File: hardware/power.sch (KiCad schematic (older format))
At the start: 56 parts, among them P1 CONN_01X02, P4 CONN_01X02, Q1 DMG4712SSS, Q2 DMG4712SSS, SW1 SPST, U10 LF33ABDT, U16 MCP1501T-30E, U17 MIC5225-5.0, U7 LT3471, U8 PDM1-S, U9 MIC5225-5.0

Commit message: Added most footprints, did non-power layout
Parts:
- removed SW1: SPST, symbol SPST
- added R55: 10k, symbol R
- added SW1: SW-SPST, 2kwMotorController:SW_SPST, symbol SW-SPST
- C62, C63: footprint (none) -> Capacitors_SMD:C_0603
- P1: value CONN_01X02 -> CONN_01X02_CBAT; footprint (none) -> 2kwMotorController:TERM_2P_2-5_1990009
- P4: value CONN_01X02 -> CONN_01X02_FAN; footprint (none) -> 2kwMotorController:TERM_2P_2-5_1990009
- R38, R39, R40, R41, R42, R54: footprint (none) -> Resistors_SMD:R_0603
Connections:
- wire segments 134 -> 137
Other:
- moved on the sheet: P1, Q1, R9
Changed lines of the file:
@@
 L CONN_01X02 P1
 U 1 1 597A960B
-P 800 1400
-F 0 "P1" H 800 1550 50  0000 C CNN
-F 1 "CONN_01X02" V 900 1400 50  0000 C CNN
-F 2 "" H 800 1400 50  0001 C CNN
-F 3 "" H 800 1400 50  0000 C CNN
-	1    800  1400
+P 950 1400
+F 0 "P1" H 950 1550 50  0000 C CNN
+F 1 "CONN_01X02_CBAT" V 1050 1400 50  0000 C CNN
+F 2 "2kwMotorController:TERM_2P_2-5_1990009" H 950 1400 50  0001 C CNN
+F 3 "" H 950 1400 50  0000 C CNN
+	1    950  1400
 	-1   0    0    -1
 $EndComp
-Text Notes 650  1050 0    60   ~ 12
+Text Notes 800  1050 0    60   ~ 12
 Battery Input\n9V max / 5V min\n750 mA max load\n2S LiPo Recommended
-$Comp
-L SPST SW1
-U 1 1 597A9A9C
-P 1550 1350
-F 0 "SW1" H 1550 1450 50  0000 C CNN
-F 1 "SPST" H 1550 1250 50  0000 C CNN
-F 2 "" H 1550 1350 50  0001 C CNN
-F 3 "" H 1550 1350 50  0000 C CNN
-	1    1550 1350
-	1    0    0    -1
-$EndComp
 $Comp
 L GND #PWR021
 U 1 1 597A9AEF
-P 2550 7350
-F 0 "#PWR021" H 2550 7100 50  0001 C CNN
-F 1 "GND" H 2550 7200 50  0000 C CNN
-F 2 "" H 2550 7350 50  0000 C CNN
-F 3 "" H 2550 7350 50  0000 C CNN
-	1    2550 7350
+P 2350 7350
+F 0 "#PWR021" H 2350 7100 50  0001 C CNN
+F 1 "GND" H 2350 7200 50  0000 C CNN
+F 2 "" H 2350 7350 50  0000 C CNN
+F 3 "" H 2350 7350 50  0000 C CNN
+	1    2350 7350
 	1    0    0    -1
 $EndComp
@@
 L R R9
 U 1 1 59870B9B
-P 2100 6800
-F 0 "R9" V 2180 6800 50  0000 C CNN
-F 1 "100" V 2100 6800 50  0000 C CNN
-F 2 "Resistors_SMD:R_0603" V 2030 6800 50  0001 C CNN
-F 3 "" H 2100 6800 50  0000 C CNN
-	1    2100 6800
-	1    0    0    -1
-$EndComp
-Text Notes 2350 7750 2    59   ~ 12
+P 1850 6750
+F 0 "R9" V 1930 6750 50  0000 C CNN
+F 1 "100" V 1850 6750 50  0000 C CNN
+F 2 "Resistors_SMD:R_0603" V 1780 6750 50  0001 C CNN
+F 3 "" H 1850 6750 50  0000 C CNN
+	1    1850 6750
+	-1   0    0    1
+$EndComp
+Text Notes 2500 7750 2    59   ~ 12
 REVERSE POLARITY PROTECTION\n14mW max - no heatsink needed
 Text Notes 8100 5650 0    60   ~ 12
@@
 F 0 "R38" V 4830 2300 50  0000 C CNN
 F 1 "220" V 4750 2300 50  0000 C CNN
-F 2 "" V 4680 2300 50  0001 C CNN
+F 2 "Resistors_SMD:R_0603" V 4680 2300 50  0001 C CNN
 F 3 "" H 4750 2300 50  0000 C CNN
 	1    4750 2300
@@
 F 0 "R39" V 6530 5000 50  0000 C CNN
 F 1 "2.2k" V 6450 5000 50  0000 C CNN
-F 2 "" V 6380 5000 50  0001 C CNN
+F 2 "Resistors_SMD:R_0603" V 6380 5000 50  0001 C CNN
 F 3 "" H 6450 5000 50  0000 C CNN
 	1    6450 5000
@@
 F 0 "R40" V 6530 6300 50  0000 C CNN
 F 1 "2.2k" V 6450 6300 50  0000 C CNN
-F 2 "" V 6380 6300 50  0001 C CNN
+F 2 "Resistors_SMD:R_0603" V 6380 6300 50  0001 C CNN
 F 3 "" H 6450 6300 50  0000 C CNN
 	1    6450 6300
@@
 $EndComp
 $Comp
-L GND #PWR046
+L GND #PWR045
 U 1 1 59BF3490
 P 2500 3500
-F 0 "#PWR046" H 2500 3250 50  0001 C CNN
+F 0 "#PWR045" H 2500 3250 50  0001 C CNN
 F 1 "GND" H 2500 3350 50  0000 C CNN
 F 2 "" H 2500 3500 50  0000 C CNN
@@
 $EndComp
 Wire Wire Line
-	1050 1350 1000 1350
-Wire Wire Line
-	1000 1450 1100 1450
-Wire Wire Line
-	2050 1350 3500 1350
+	1150 1350 3500 1350
+Wire Wire Line
+	1150 1450 1250 1450
 Wire Wire Line
 	2550 1350 2550 1250
@@
 	8750 4750 8750 4800
 Wire Wire Line
-	8750 5100 8750 5150
+	8750 5150 8750 5100
 Wire Wire Line
 	8200 5150 9200 5150
@@
 Connection ~ 8750 4300
 Wire Wire Line
-	1100 1450 1100 7350
-Wire Wire Line
-	1100 7300 1900 7300
-Wire Wire Line
-	2550 7300 2550 7350
-Wire Wire Line
-	2100 1300 2100 6650
+	1250 1450 1250 7350
+Wire Wire Line
+	1250 7300 1650 7300
+Wire Wire Line
+	2350 6950 2350 7350
+Wire Wire Line
+	2100 1300 2100 6550
 Connection ~ 2100 1350
 Wire Wire Line
-	2100 7000 2100 6950
-Wire Wire Line
-	2300 7300 2550 7300
+	2050 7300 2350 7300
 Wire Notes Line
 	7900 4650 7900 5750
@@
 Connection ~ 2550 1350
 Connection ~ 3150 1350
-Connection ~ 2100 6550
 Connection ~ 2100 4350
 Connection ~ 5850 4350
 Wire Wire Line
-	2400 5850 2100 5850
+	1850 5850 2400 5850
 Connection ~ 2100 5850
 Wire Wire Line
@@
 	2500 3450 2750 3450
 $Comp
-L +5V #PWR047
+L +5V #PWR046
 U 1 1 59BF5180
 P 3800 3100
-F 0 "#PWR047" H 3800 2950 50  0001 C CNN
+F 0 "#PWR046" H 3800 2950 50  0001 C CNN
 F 1 "+5V" H 3800 3240 50  0000 C CNN
 F 2 "" H 3800 3100 50  0000 C CNN
@@
 Encoder supply
 $Comp
-L GNDCBAT #PWR048
+L GNDCBAT #PWR047
 U 1 1 59C0C795
-P 1100 7350
-F 0 "#PWR048" H 1100 7100 50  0001 C CNN
-F 1 "GNDCBAT" H 1100 7200 50  0000 C CNN
-F 2 "" H 1100 7350 50  0000 C CNN
-F 3 "" H 1100 7350 50  0000 C CNN
-	1    1100 7350
-	1    0    0    -1
-$EndComp
-Connection ~ 1100 7300
+P 1250 7350
+F 0 "#PWR047" H 1250 7100 50  0001 C CNN
+F 1 "GNDCBAT" H 1250 7200 50  0000 C CNN
+F 2 "" H 1250 7350 50  0000 C CNN
+F 3 "" H 1250 7350 50  0000 C CNN
+	1    1250 7350
+	1    0    0    -1
+$EndComp
+Connection ~ 1250 7300
 Wire Wire Line
 	10150 2200 10150 2400
 $Comp
-L GND #PWR049
+L GND #PWR048
 U 1 1 59C60D75
 P 10150 2400
-F 0 "#PWR049" H 10150 2150 50  0001 C CNN
+F 0 "#PWR048" H 10150 2150 50  0001 C CNN
 F 1 "GND" H 10150 2250 50  0000 C CNN
 F 2 "" H 10150 2400 50  0000 C CNN
@@
 P 9650 1550
 F 0 "P4" H 9650 1700 50  0000 C CNN
-F 1 "CONN_01X02" V 9750 1550 50  0000 C CNN
-F 2 "" H 9650 1550 50  0001 C CNN
+F 1 "CONN_01X02_FAN" V 9750 1550 50  0000 C CNN
+F 2 "2kwMotorController:TERM_2P_2-5_1990009" H 9650 1550 50  0001 C CNN
 F 3 "" H 9650 1550 50  0000 C CNN
 	1    9650 1550
@@
 	10150 1700 10150 1800
 $Comp
-L +12V #PWR050
+L +12V #PWR049
 U 1 1 59C60D8A
 P 10150 1300
-F 0 "#PWR050" H 10150 1150 50  0001 C CNN
+F 0 "#PWR049" H 10150 1150 50  0001 C CNN
 F 1 "+12V" H 10150 1440 50  0000 C CNN
 F 2 "" H 10150 1300 50  0000 C CNN
@@
 F 0 "R41" V 9680 2000 50  0000 C CNN
 F 1 "100" V 9600 2000 50  0000 C CNN
-F 2 "" V 9530 2000 50  0001 C CNN
+F 2 "Resistors_SMD:R_0603" V 9530 2000 50  0001 C CNN
 F 3 "" H 9600 2000 50  0000 C CNN
 	1    9600 2000
@@
 F 0 "R42" V 9880 2200 50  0000 C CNN
 F 1 "10k" V 9800 2200 50  0000 C CNN
-F 2 "" V 9730 2200 50  0001 C CNN
+F 2 "Resistors_SMD:R_0603" V 9730 2200 50  0001 C CNN
 F 3 "" H 9800 2200 50  0000 C CNN
 	1    9800 2200
@@
 L NMOS_8PIN Q1
 U 1 1 59BDA6D3
-P 2100 7200
-F 0 "Q1" V 2100 7450 50  0000 R CNN
-F 1 "DMG4712SSS" V 2350 7400 50  0000 R CNN
-F 2 "Housings_SOIC:SOIC-8_3.9x4.9mm_Pitch1.27mm" H 2300 7300 50  0001 C CNN
-F 3 "" H 2100 7200 50  0000 C CNN
-	1    2100 7200
+P 1850 7200
+F 0 "Q1" V 1850 7450 50  0000 R CNN
+F 1 "DMG4712SSS" V 2100 7400 50  0000 R CNN
+F 2 "Housings_SOIC:SOIC-8_3.9x4.9mm_Pitch1.27mm" H 2050 7300 50  0001 C CNN
+F 3 "" H 1850 7200 50  0000 C CNN
+	1    1850 7200
 	0    -1   1    0
 $EndComp
@@
 F 0 "C62" H 7225 4650 50  0000 L CNN
 F 1 "2.2u" H 7225 4450 50  0000 L CNN
-F 2 "" H 7238 4400 50  0001 C CNN
+F 2 "Capacitors_SMD:C_0603" H 7238 4400 50  0001 C CNN
 F 3 "" H 7200 4550 50  0000 C CNN
 	1    7200 4550
@@
 F 0 "C63" H 8375 4650 50  0000 L CNN
 F 1 "2.2u" H 8375 4450 50  0000 L CNN
-F 2 "" H 8388 4400 50  0001 C CNN
+F 2 "Capacitors_SMD:C_0603" H 8388 4400 50  0001 C CNN
 F 3 "" H 8350 4550 50  0000 C CNN
 	1    8350 4550
@@
 F 0 "R54" V 8630 4950 50  0000 C CNN
 F 1 "2.2k" V 8550 4950 50  0000 C CNN
-F 2 "" V 8480 4950 50  0001 C CNN
+F 2 "Resistors_SMD:R_0603" V 8480 4950 50  0001 C CNN
 F 3 "" H 8550 4950 50  0000 C CNN
 	1    8550 4950
@@
 Connection ~ 8550 5150
 $Comp
-L GND #PWR?
+L GND #PWR050
 U 1 1 59BAC5F2
 P 3800 3550
-F 0 "#PWR?" H 3800 3300 50  0001 C CNN
+F 0 "#PWR050" H 3800 3300 50  0001 C CNN
 F 1 "GND" H 3800 3400 50  0000 C CNN
 F 2 "" H 3800 3550 50  0000 C CNN
@@
 	1    0    0    -1
 $EndComp
+Wire Wire Line
+	1850 6900 1850 7000
+$Comp
+L SW-SPST SW1
+U 1 1 59BC78B3
+P 1850 6200
+F 0 "SW1" H 1850 6300 50  0000 C CNN
+F 1 "SW-SPST" H 1850 6100 50  0000 C CNN
+F 2 "2kwMotorController:SW_SPST" H 1850 6200 50  0001 C CNN
+F 3 "" H 1850 6200 50  0000 C CNN
+	1    1850 6200
+	0    1    1    0
+$EndComp
+Wire Wire Line
+	1850 6600 1850 6500
+Wire Wire Line
+	1850 5900 1850 5850
+$Comp
+L R R55
+U 1 1 59BCE5FC
+P 2150 6950
+F 0 "R55" V 2230 6950 50  0000 C CNN
+F 1 "10k" V 2150 6950 50  0000 C CNN
+F 2 "" V 2080 6950 50  0001 C CNN
+F 3 "" H 2150 6950 50  0000 C CNN
+	1    2150 6950
+	0    1    1    0
+$EndComp
+Wire Wire Line
+	2350 6950 2300 6950
+Connection ~ 2350 7300
+Wire Wire Line
+	1850 6950 2000 6950
+Connection ~ 1850 6950
 $EndSCHEMATC

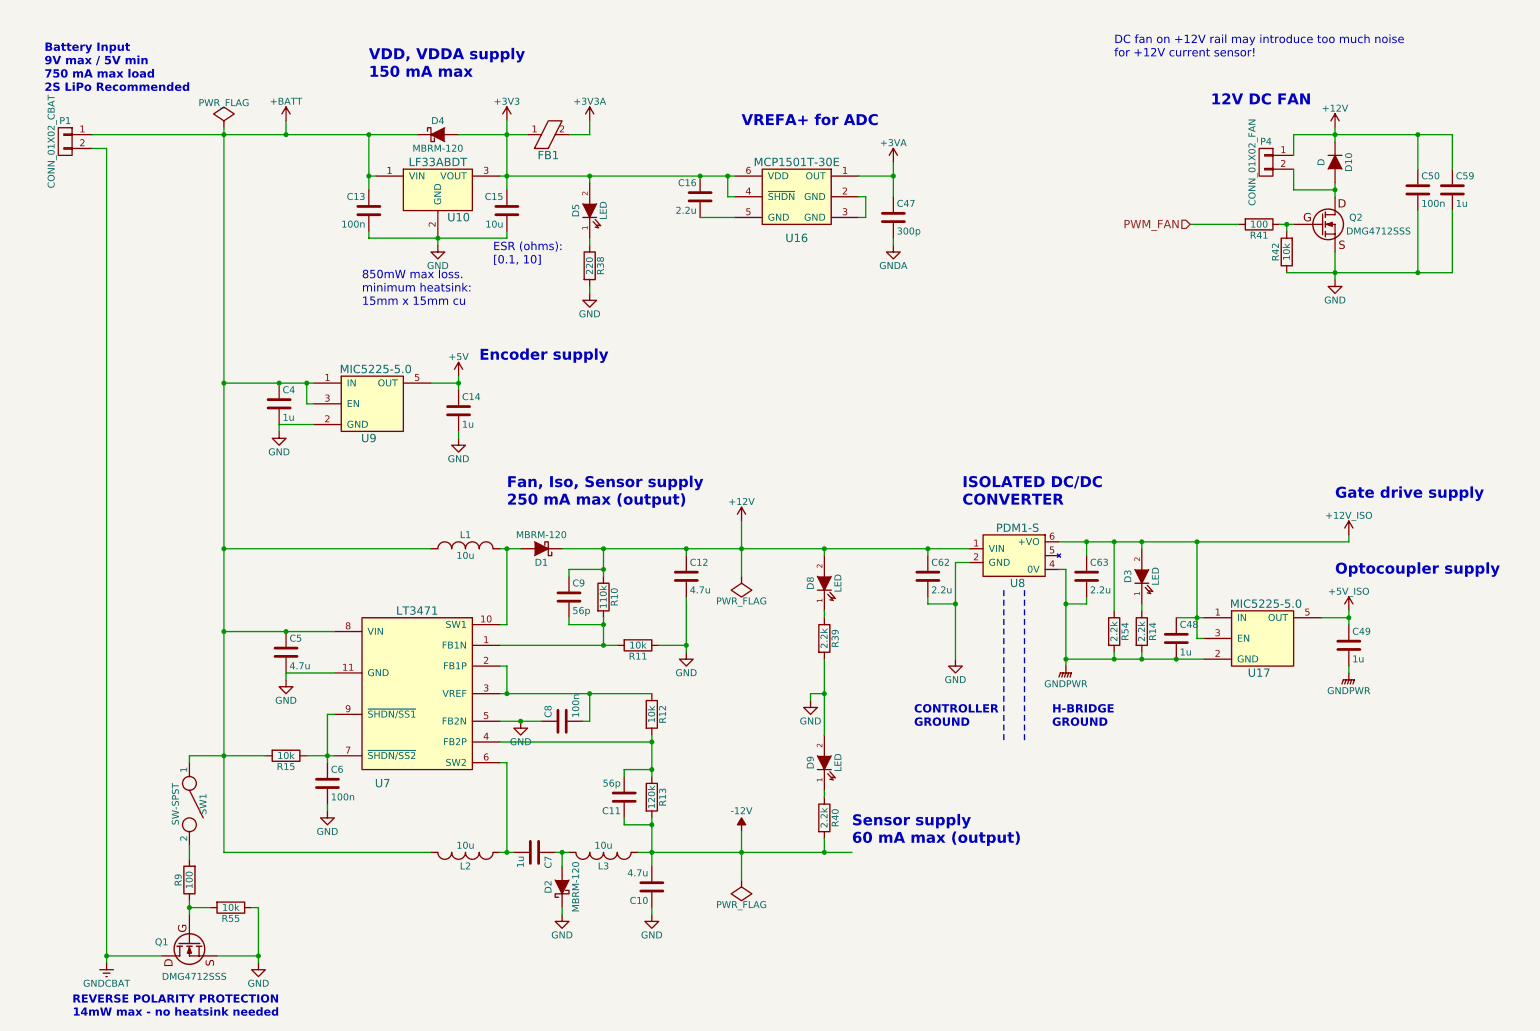
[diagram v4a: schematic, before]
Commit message: H-bridge decoupling, footprints, mechanical
- Finished H-bridge decoupling study and chose H-bridge caps
- Changed LT3471 inductors to those found in reference design,
  made footprints for them
- Swapped Si86xx isolator for Si80xx (smaller package)
- Updated heatsink footprint with correct screw sizes
- Created mechanical hole footprints (M3, M4 screws)
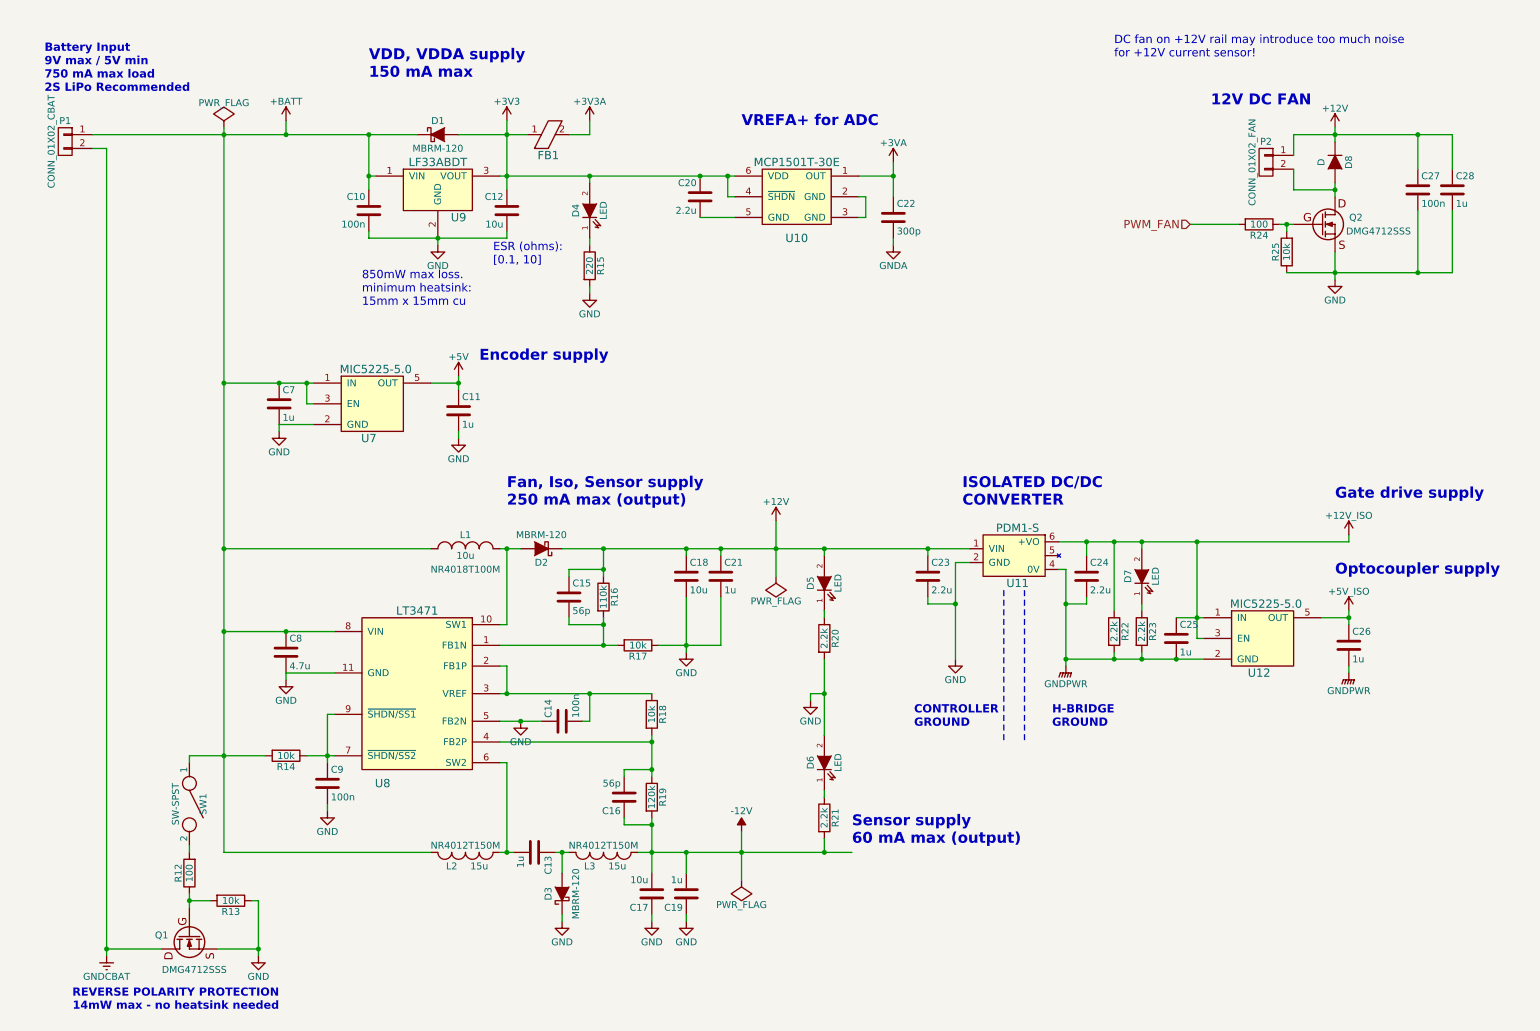
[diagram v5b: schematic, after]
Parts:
- added C19, C21: 1u, Capacitors_SMD:C_0603, symbol C
- C17: renamed from C10; value 4.7u -> 10u
- C18: renamed from C12; value 4.7u -> 10u
- L1: footprint Capacitors_SMD:C_0603 -> 2kwMotorController:INDUCTOR_NR40xx
- L2, L3: value 10u -> 15u; footprint Capacitors_SMD:C_0603 -> 2kwMotorController:INDUCTOR_NR40xx
- R13: renamed from R55; footprint (none) -> Resistors_SMD:R_0603
- renumbered C13 to C10, C14 to C11, C15 to C12, C7 to C13, C8 to C14, C9 to C15, C11 to C16, C16 to C20, C47 to C22, C62 to C23, C63 to C24, C48 to C25, C49 to C26, C50 to C27, C59 to C28, C4 to C7, C5 to C8, C6 to C9, D4 to D1, D1 to D2, D2 to D3, D5 to D4, D8 to D5, D9 to D6, D3 to D7, D10 to D8, P4 to P2, R9 to R12, R15 to R14, R38 to R15, R10 to R16, R11 to R17, R12 to R18, R13 to R19, R39 to R20, R40 to R21, R54 to R22, R14 to R23, R41 to R24, R42 to R25, U16 to U10, U8 to U11, U17 to U12, U9 to U7, U7 to U8, U10 to U9
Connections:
- net +12V: now also C21.1
- net -12V: now also C19.2
- net GND: now also C19.1, C21.2
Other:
- moved on the sheet: C17, D3, Q1, R12, R13

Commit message: Bulk cap layout, diodes, lugs, leds, trimpots
- Moved H-bridge bulk capacitors to horizontal layout
- Changed H-bridge and fan diodes to 100V schottky
- Made 4AWG lug mount footprint, added lugs to BOM
- Tweaked LED resistor values, added LEDs to BOM
- Made trimpot footprint, added trimpots to BOM
- Added snubber to ferrite bead circuit; also added FB to BOM
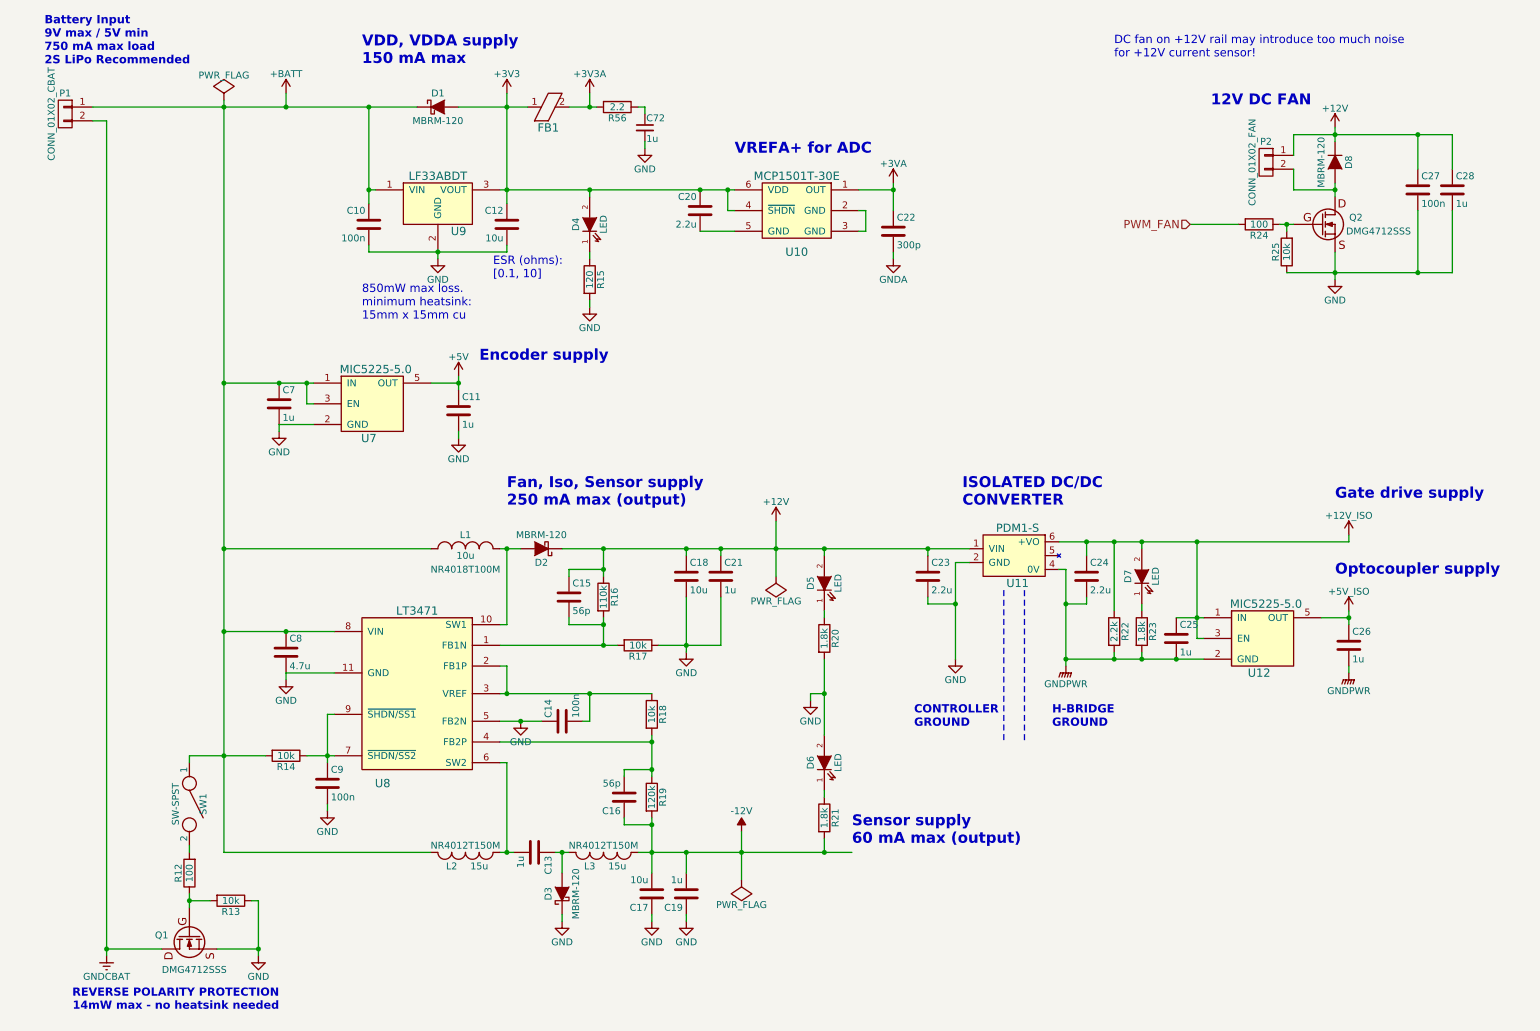
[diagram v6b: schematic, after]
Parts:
- added C72: 1u, Capacitors_SMD:C_0603, symbol C_Small
- added R56: 2.2, Resistors_SMD:R_0603, symbol R
- D1, D2, D3: footprint Diodes_SMD:SOD-123 -> 2kwMotorController:DIODE_POWERMITE
- D4, D5, D6, D7: footprint Diodes_SMD:SOD-123 -> LEDs:LED_0603
- D8: value D -> MBRM-120; footprint (none) -> 2kwMotorController:DIODE_POWERMITE
- FB1: footprint (none) -> Capacitors_SMD:C_0603
- R15: value 220 -> 120
- R20, R21, R23: value 2.2k -> 1.8k
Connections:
- net +3V3: now also R56.2
- net GND: now also C72.2
- new net: C72.1, R56.1
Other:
- moved on the sheet: C10, C12, C20, C22, D1, D4, FB1, P1, R15, U10, U9
